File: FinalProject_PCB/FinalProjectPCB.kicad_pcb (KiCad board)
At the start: 2 copper layers, 70 x 80 mm, 14 parts, among them J1 Serial Jack, J2 Conn_01x09, SW10 Nav Switch, SW5 SW_Push_Dual, SW6 SW_Push_Dual, SW7 SW_SPST, SW8 SW_Push_Dual, SW9 SW_Push_Dual, U1 ESP32-S2-DevKitC-1

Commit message: Finished PCB
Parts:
- SW7: footprint TestPoint:TestPoint_Bridge_Pitch2.54mm_Drill1.0mm -> TerminalBlock:TerminalBlock_Xinya_XY308-2.54-2P_1x02_P2.54mm_Horizontal
- moved RV1 140.8 mm to (152.5, 89.0), turned to -90 degrees
- moved LS1 94.2 mm to (142.0, 161.0)
- moved U1 74.8 mm to (140.4, 116.4), turned to 90 degrees
- moved BT1 74.1 mm to (83.0, 86.5)
- moved D1 66.3 mm to (75.5, 161.0)
- moved R1 61.2 mm to (81.0, 154.5), turned to 90 degrees
- moved SW6 46.9 mm to (137.5, 124.3)
- moved SW5 46.9 mm to (126.9, 134.8)
- moved SW8 18.4 mm to (96.5, 161.3)
- moved SW9 18.4 mm to (113.5, 161.3)
- moved SW10 3.97 mm to (87.5, 132.0)
- moved J1 3.50 mm to (126.4, 86.0)
- moved SW7 3.15 mm to (77.0, 85.5), turned to -90 degrees
- moved J2 3.10 mm to (98.3, 86.0)
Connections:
- BT1 pad 1: GND -> 5V-IN
- BT1 pad 2: 5V-IN -> GND
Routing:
- net GND: track 0.00 -> 338.2 mm
- net HOME: track 0.00 -> 104.5 mm
- net B: track 0.00 -> 104.0 mm, vias 0 -> 1
- net 3V3: track 0.00 -> 95.4 mm
- net RIGHT: track 0.00 -> 91.3 mm
- net DOWN: track 0.00 -> 81.3 mm
- net SELECT: track 0.00 -> 80.1 mm
- net VOLUME: track 0.00 -> 68.0 mm, vias 0 -> 2
- net LEFT: track 0.00 -> 58.8 mm, vias 0 -> 2
- net RESET: track 0.00 -> 57.2 mm
- net CS: track 0.00 -> 54.9 mm
- net PowerLED: track 0.00 -> 53.0 mm
- net DC/RS: track 0.00 -> 52.4 mm, vias 0 -> 1
- net PIEZO: track 0.00 -> 48.3 mm, vias 0 -> 2
- net CENTER: track 0.00 -> 46.3 mm
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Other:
- board size 70 x 80 mm -> 80 x 90 mm
- board text added: "August & Ethan"
- board text added: "RX"
- board text added: "TX"

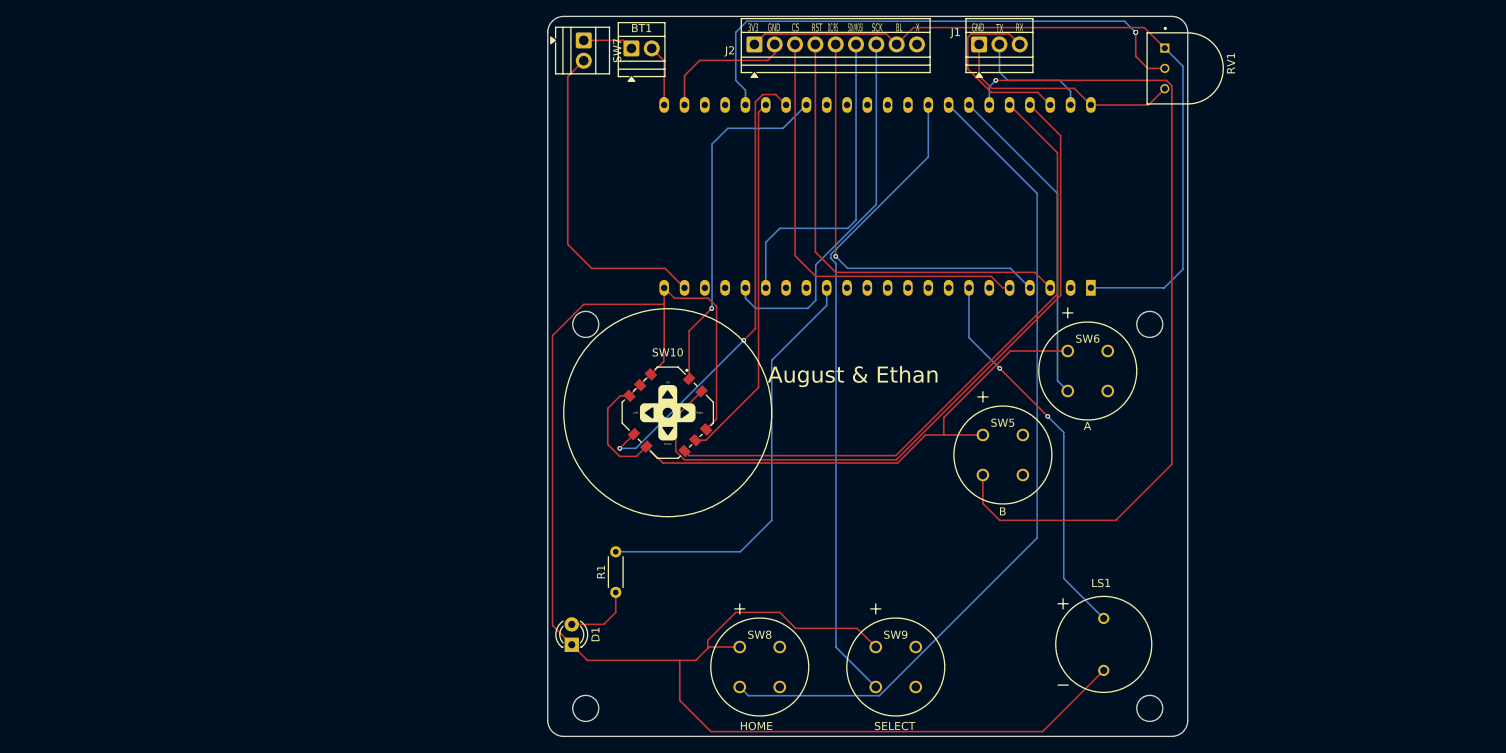
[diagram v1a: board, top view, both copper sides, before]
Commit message: added 3d Model
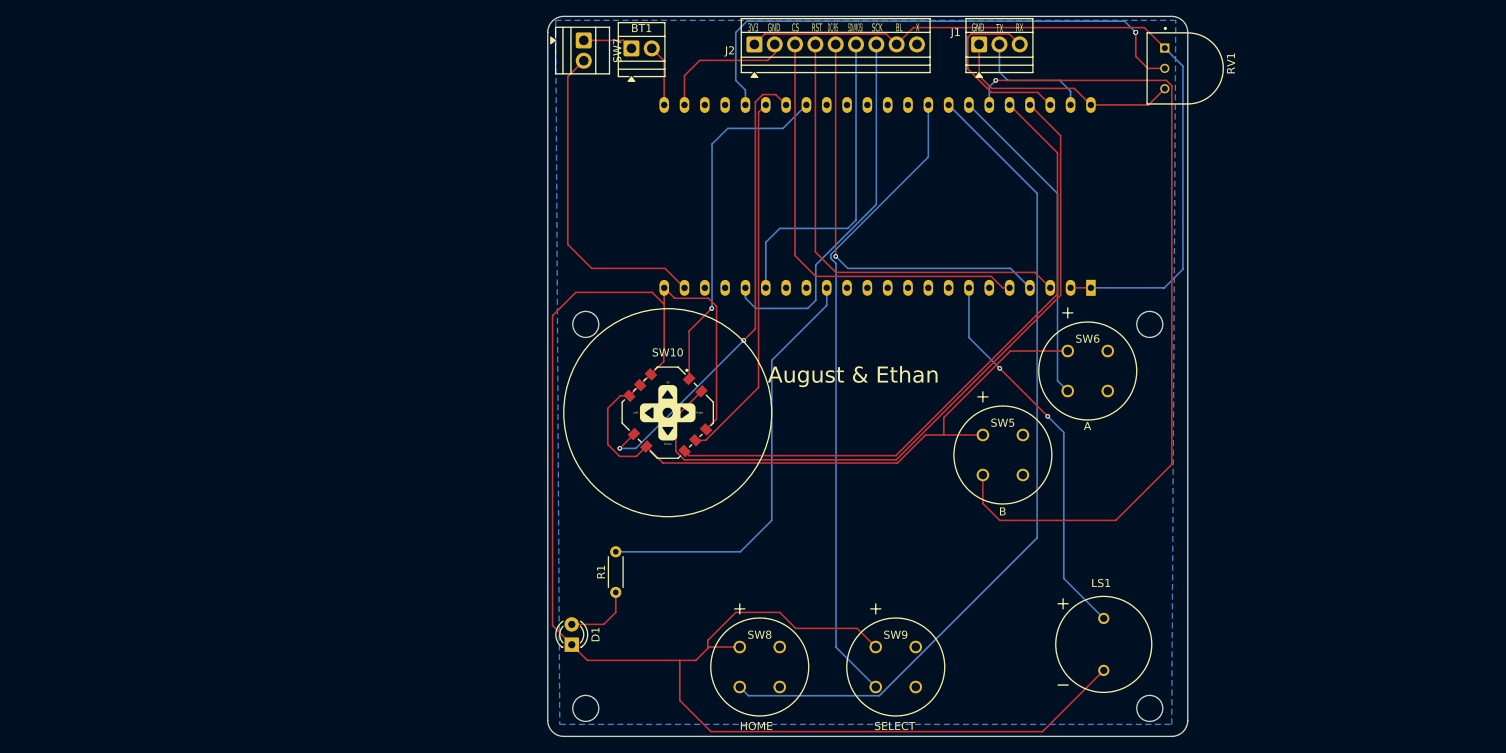
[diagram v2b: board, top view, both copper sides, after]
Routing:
- net GND: track 338.2 -> 340.9 mm
- net 3V3: track 95.4 -> 98.0 mm
- added copper zone on B.Cu, net GND
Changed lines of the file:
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@@
 			(outputformat 1)
 			(mirror no)
-			(drillshape 1)
+			(drillshape 0)
 			(scaleselection 1)
-			(outputdirectory "")
+			(outputdirectory "Manufacturing Files/")
 		)
 	)
@@
 	)
 	(segment
+		(start 76 117)
+		(end 85.5548 117)
+		(width 0.2)
+		(layer "F.Cu")
+		(net 2)
+	)
+	(segment
 		(start 122 134.825505)
 		(end 119.724981 134.825505)
@@
 	)
 	(segment
-		(start 73.101 122.399)
-		(end 77 118.5)
-		(width 0.2)
-		(layer "F.Cu")
-		(net 2)
-	)
-	(segment
 		(start 84.052854 128.588304)
 		(end 85.396357 127.244802)
@@
 	)
 	(segment
+		(start 75.5 161.04)
+		(end 73.101 158.641)
+		(width 0.2)
+		(layer "F.Cu")
+		(net 2)
+	)
+	(segment
 		(start 92.290648 134.139093)
 		(end 93.601 132.828741)
@@
 	)
 	(segment
+		(start 85.5548 117)
+		(end 87.0548 118.5)
+		(width 0.2)
+		(layer "F.Cu")
+		(net 2)
+	)
+	(segment
 		(start 100.872858 86)
 		(end 100.872858 87.127142)
@@
 	)
 	(segment
-		(start 77 118.5)
-		(end 87.0548 118.5)
-		(width 0.2)
-		(layer "F.Cu")
-		(net 2)
-	)
-	(segment
 		(start 147.6 93.57)
 		(end 140.39208 93.57)
@@
 	)
 	(segment
+		(start 73.101 119.899)
+		(end 76 117)
+		(width 0.2)
+		(layer "F.Cu")
+		(net 2)
+	)
+	(segment
 		(start 96.5 161.325505)
 		(end 92.674495 161.325505)
@@
 	)
 	(segment
+		(start 73.101 158.641)
+		(end 73.101 119.899)
+		(width 0.2)
+		(layer "F.Cu")
+		(net 2)
+	)
+	(segment
 		(start 116.226893 138.323593)
 		(end 86.893852 138.323593)
@@
 	)
 	(segment
-		(start 73.101 158.641)
-		(end 73.101 122.399)
-		(width 0.2)
-		(layer "F.Cu")
-		(net 2)
-	)
-	(segment
 		(start 134.351 171.899)
 		(end 92.899 171.899)
@@
 	)
 	(segment
-		(start 75.5 161.04)
-		(end 73.101 158.641)
-		(width 0.2)
-		(layer "F.Cu")
-		(net 2)
-	)
-	(segment
 		(start 111.174495 159)
 		(end 103.5 159)
@@
 	)
 	(segment
+		(start 140.39208 116.43)
+		(end 137.85208 116.43)
+		(width 0.2)
+		(layer "F.Cu")
+		(net 8)
+	)
+	(segment
 		(start 118.213858 83.899)
 		(end 147.069 83.899)
@@
 		(net 44)
 	)
+	(zone
+		(net 2)
+		(net_name "GND")
+		(layer "B.Cu")
+		(hatch edge 0.5)
+		(connect_pads
+			(clearance 0.5)
+		)
+		(min_thickness 0.25)
+		(filled_areas_thickness no)
+		(fill yes
+			(thermal_gap 0.5)
+			(thermal_bridge_width 0.5)
+		)
+		(polygon
+			(pts
+				(xy 151 83) (xy 73.5 83) (xy 74 171) (xy 150.5 171)
+			)
+		)
+	)
 	(group ""
